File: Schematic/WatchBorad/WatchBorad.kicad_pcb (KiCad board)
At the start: 4 copper layers, 35 x 35 mm, 114 parts, among them J1 Conn_01x07_Female, J3 TYPE-C-31-M-17, M1 Motor_DC, SW1 SW_Push, SW2 SW_Push, SW3 SW_Push, SW4 SW_Push, SW5 SW_Push, U1 LSM6DSLTR, U10 TPS62740DSST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

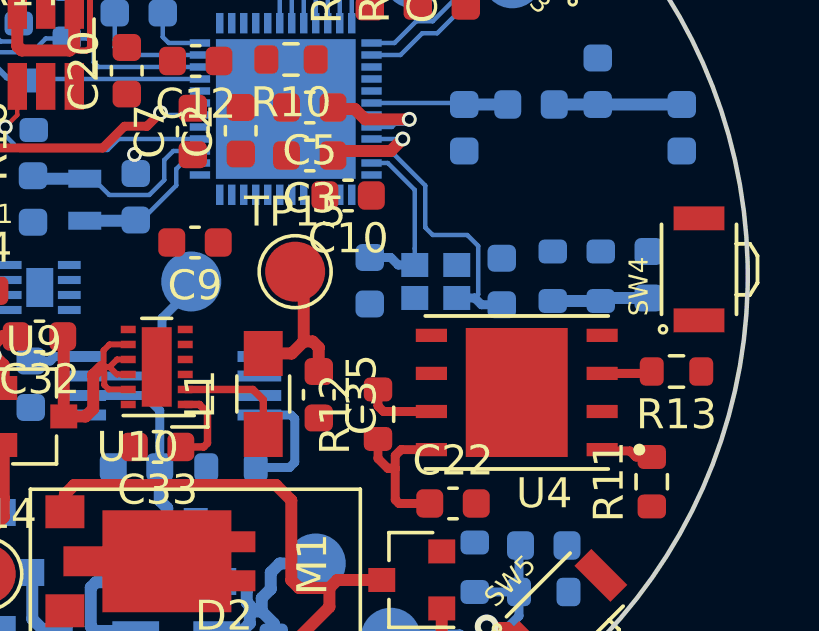
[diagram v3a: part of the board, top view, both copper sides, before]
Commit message: Added route for SPI-FLASH
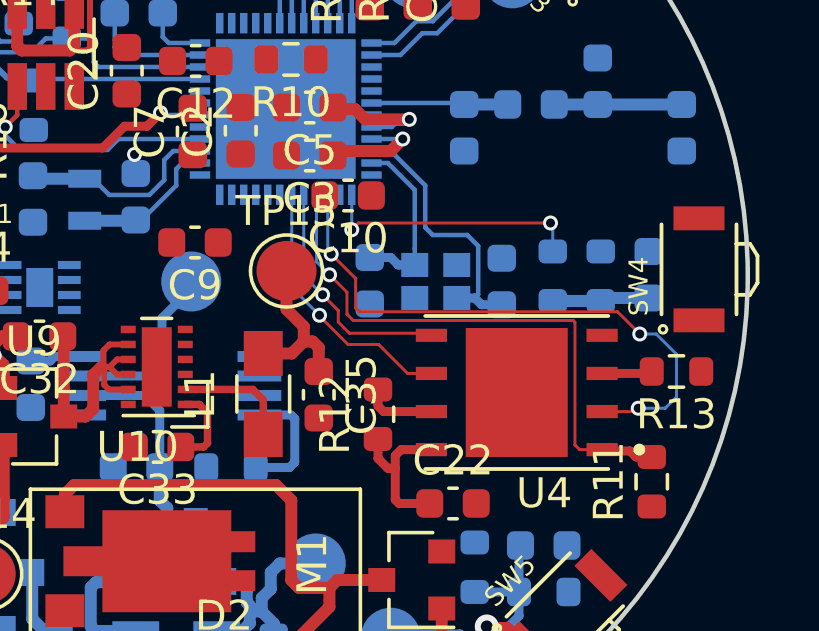
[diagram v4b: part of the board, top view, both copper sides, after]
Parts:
- moved TP15 0.29 mm to (91.0, 88.8)
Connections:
- U2 pad 42: /DCDC&PB/Enable_motor -> /MCU/FLASH_SCK
- U2 pad 43: /MCU/FLASH_SCK -> /DCDC&PB/Enable_motor
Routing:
- net /MCU/FLASH_MISO: track 0.00 -> 19.6 mm, vias 0 -> 3
- net /MCU/FLASH_CS: track 1.76 -> 18.9 mm, vias 0 -> 1
- net /MCU/FLASH_SCK: track 0.00 -> 8.95 mm, vias 0 -> 1
- net /MCU/PB_4_MCU: track 0.00 -> 8.86 mm, vias 0 -> 2
- net /MCU/FLASH_MOSI: track 0.00 -> 8.01 mm, vias 0 -> 1
- net +3V3: track 12.6 -> 13.2 mm
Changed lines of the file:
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@@
     (thickness 1.6)
     (drawings 1)
-    (tracks 450)
+    (tracks 506)
     (zones 0)
     (modules 114)
@@
   )
   (setup
-    (last_trace_width 0.15)
+    (last_trace_width 0.1)
     (user_trace_width 0.1)
     (user_trace_width 0.15)
@@
   )
   (module TestPoint:TestPoint_Pad_D2.0mm (layer F.Cu)
-    (at 91.313 88.773)
+    (at 91.025 88.75)
     (descr "SMD pad as test Point, diameter 2.0mm")
     (tags "test point SMD pad")
@@
       (net 70 "Net-(U2-Pad44)"))
     (pad 43 smd rect (at -0.2 2.86) (size 0.25 0.68) (layers B.Cu B.Paste B.Mask)
-      (net 39 /MCU/FLASH_SCK))
-    (pad 42 smd rect (at 0.2 2.86) (size 0.25 0.68) (layers B.Cu B.Paste B.Mask)
       (net 37 /DCDC&PB/Enable_motor))
+    (pad 42 smd rect (at 0.2 2.86) (size 0.25 0.68) (layers B.Cu B.Paste B.Mask)
+      (net 39 /MCU/FLASH_SCK))
     (pad 41 smd rect (at 0.6 2.86) (size 0.25 0.68) (layers B.Cu B.Paste B.Mask)
       (net 38 /MCU/FLASH_MOSI))
@@
   (segment (start 91.9 91.1) (end 92.1 91.3) (width 0.4) (layer F.Cu) (net 1))
   (segment (start 91.6 89.06) (end 91.313 88.773) (width 0.4) (layer F.Cu) (net 1))
-  (segment (start 91.6 91.1) (end 91.6 89.06) (width 0.4) (layer F.Cu) (net 1))
   (segment (start 94.775 96.5) (end 95.8 96.5) (width 0.3) (layer F.Cu) (net 1))
   (segment (start 94.65 96.375) (end 94.775 96.5) (width 0.3) (layer F.Cu) (net 1))
@@
   (segment (start 94.65 95.325) (end 94.65 96.375) (width 0.3) (layer F.Cu) (net 1))
   (segment (start 94.65 94.9) (end 94.65 95.325) (width 0.3) (layer F.Cu) (net 1))
+  (segment (start 91.025 88.75) (end 91.025 90.025) (width 0.4) (layer F.Cu) (net 1))
+  (segment (start 91.6 90.6) (end 91.6 91.1) (width 0.4) (layer F.Cu) (net 1))
+  (segment (start 91.025 90.025) (end 91.6 90.6) (width 0.4) (layer F.Cu) (net 1))
   (via (at 85.2 77.7) (size 0.5) (drill 0.3) (layers F.Cu B.Cu) (net 2))
   (segment (start 85.3 77.8) (end 85.2 77.7) (width 0.15) (layer B.Cu) (net 2))
@@
   (segment (start 80 93.5) (end 80 92.9) (width 0.4) (layer F.Cu) (net 19))
   (segment (start 79.9 93.6) (end 80 93.5) (width 0.4) (layer F.Cu) (net 19))
+  (via (at 99.825 87.15) (size 0.5) (drill 0.3) (layers F.Cu B.Cu) (net 21))
+  (segment (start 99.9 87.225) (end 99.825 87.15) (width 0.1) (layer B.Cu) (net 21))
+  (segment (start 99.9 88.1) (end 99.9 87.225) (width 0.1) (layer B.Cu) (net 21))
+  (via (at 93.2 87.375) (size 0.5) (drill 0.3) (layers F.Cu B.Cu) (net 21))
+  (segment (start 93.425 87.15) (end 93.2 87.375) (width 0.1) (layer F.Cu) (net 21))
+  (segment (start 99.825 87.15) (end 93.425 87.15) (width 0.1) (layer F.Cu) (net 21))
+  (segment (start 93.2 87.375) (end 93.2 86.21) (width 0.1) (layer B.Cu) (net 21))
   (segment (start 83.95 81.25) (end 83.95 79.9) (width 0.4) (layer F.Cu) (net 23))
   (segment (start 83.8 81.4) (end 83.95 81.25) (width 0.4) (layer F.Cu) (net 23))
@@
   (segment (start 94.575 100.9) (end 94.5 100.975) (width 0.4) (layer B.Cu) (net 37))
   (segment (start 96.8 100.9) (end 94.575 100.9) (width 0.4) (layer B.Cu) (net 37))
+  (via (at 92.227233 89.542614) (size 0.5) (drill 0.3) (layers F.Cu B.Cu) (net 38))
+  (segment (start 91.6 88.915381) (end 92.227233 89.542614) (width 0.1) (layer B.Cu) (net 38))
+  (segment (start 91.6 86.21) (end 91.6 88.915381) (width 0.1) (layer B.Cu) (net 38))
+  (segment (start 92.227233 89.542614) (end 92.75 90.065381) (width 0.1) (layer F.Cu) (net 38))
+  (segment (start 92.75 90.065381) (end 92.75 90.45) (width 0.1) (layer F.Cu) (net 38))
+  (segment (start 92.75 90.45) (end 93.125 90.825) (width 0.1) (layer F.Cu) (net 38))
+  (segment (start 95.785 90.825) (end 95.855 90.895) (width 0.1) (layer F.Cu) (net 38))
+  (segment (start 93.125 90.825) (end 95.785 90.825) (width 0.1) (layer F.Cu) (net 38))
+  (segment (start 95.855 92.165) (end 95.065 92.165) (width 0.1) (layer F.Cu) (net 39))
+  (segment (start 95.065 92.165) (end 94.1 91.2) (width 0.1) (layer F.Cu) (net 39))
+  (segment (start 94.1 91.2) (end 93.075 91.2) (width 0.1) (layer F.Cu) (net 39))
+  (via (at 92.125 90.225) (size 0.5) (drill 0.3) (layers F.Cu B.Cu) (net 39))
+  (segment (start 92.125 90.25) (end 92.125 90.225) (width 0.1) (layer F.Cu) (net 39))
+  (segment (start 93.075 91.2) (end 92.125 90.25) (width 0.1) (layer F.Cu) (net 39))
+  (segment (start 92.125 90.225) (end 91.2 89.3) (width 0.1) (layer B.Cu) (net 39))
+  (segment (start 91.2 87.05) (end 91.2 86.21) (width 0.1) (layer B.Cu) (net 39))
+  (segment (start 91.2 89.3) (end 91.2 87.05) (width 0.1) (layer B.Cu) (net 39))
+  (via (at 102.75 93.325) (size 0.5) (drill 0.3) (layers F.Cu B.Cu) (net 40))
+  (segment (start 102.64 93.435) (end 102.75 93.325) (width 0.1) (layer F.Cu) (net 40))
+  (segment (start 101.545 93.435) (end 102.64 93.435) (width 0.1) (layer F.Cu) (net 40))
+  (segment (start 102.75 93.325) (end 103.65 93.325) (width 0.1) (layer B.Cu) (net 40))
+  (segment (start 103.65 93.325) (end 104.025 92.95) (width 0.1) (layer B.Cu) (net 40))
+  (segment (start 104.025 92.95) (end 104.025 91.525) (width 0.1) (layer B.Cu) (net 40))
+  (via (at 102.8 90.85) (size 0.5) (drill 0.3) (layers F.Cu B.Cu) (net 40))
+  (segment (start 103.35 90.85) (end 102.8 90.85) (width 0.1) (layer B.Cu) (net 40))
+  (segment (start 104.025 91.525) (end 103.35 90.85) (width 0.1) (layer B.Cu) (net 40))
+  (segment (start 102.8 90.85) (end 102.05999 90.10999) (width 0.1) (layer F.Cu) (net 40))
+  (segment (start 93.45999 90.10999) (end 93.33002 89.98002) (width 0.1) (layer F.Cu) (net 40))
+  (segment (start 102.05999 90.10999) (end 93.45999 90.10999) (width 0.1) (layer F.Cu) (net 40))
+  (segment (start 93.33002 89.98002) (end 93.33002 89.25502) (width 0.1) (layer F.Cu) (net 40))
+  (via (at 92.515 88.187136) (size 0.5) (drill 0.3) (layers F.Cu B.Cu) (net 40))
+  (segment (start 93.33002 89.002156) (end 92.515 88.187136) (width 0.1) (layer F.Cu) (net 40))
+  (segment (start 93.33002 89.25502) (end 93.33002 89.002156) (width 0.1) (layer F.Cu) (net 40))
+  (segment (start 92.4 88.072136) (end 92.4 86.21) (width 0.1) (layer B.Cu) (net 40))
+  (segment (start 92.515 88.187136) (end 92.4 88.072136) (width 0.1) (layer B.Cu) (net 40))
   (segment (start 103.2 94.95) (end 102.675 94.95) (width 0.3) (layer F.Cu) (net 41))
   (segment (start 102.675 94.95) (end 102.475 94.75) (width 0.3) (layer F.Cu) (net 41))
   (segment (start 101.59 94.75) (end 101.545 94.705) (width 0.3) (layer F.Cu) (net 41))
   (segment (start 102.475 94.75) (end 101.59 94.75) (width 0.3) (layer F.Cu) (net 41))
+  (via (at 92.459403 88.876862) (size 0.5) (drill 0.3) (layers F.Cu B.Cu) (net 41))
+  (segment (start 92.459403 88.876862) (end 92.025 88.442459) (width 0.1) (layer B.Cu) (net 41))
+  (segment (start 92.025 86.235) (end 92 86.21) (width 0.1) (layer B.Cu) (net 41))
+  (segment (start 92.025 88.442459) (end 92.025 86.235) (width 0.1) (layer B.Cu) (net 41))
+  (segment (start 93.04001 89.457469) (end 92.459403 88.876862) (width 0.1) (layer F.Cu) (net 41))
+  (segment (start 93.04001 90.19001) (end 93.04001 89.457469) (width 0.1) (layer F.Cu) (net 41))
+  (segment (start 93.25 90.4) (end 93.04001 90.19001) (width 0.1) (layer F.Cu) (net 41))
+  (segment (start 100.582002 90.4) (end 93.25 90.4) (width 0.1) (layer F.Cu) (net 41))
+  (segment (start 100.640001 90.457999) (end 100.582002 90.4) (width 0.1) (layer F.Cu) (net 41))
+  (segment (start 100.640001 94.55) (end 100.640001 90.457999) (width 0.1) (layer F.Cu) (net 41))
+  (segment (start 100.795001 94.705) (end 100.640001 94.55) (width 0.1) (layer F.Cu) (net 41))
+  (segment (start 101.545 94.705) (end 100.795001 94.705) (width 0.1) (layer F.Cu) (net 41))
   (segment (start 88.14 84.35) (end 85.425 84.35) (width 0.15) (layer B.Cu) (net 42))
   (via (at 81.65 83.95) (size 0.5) (drill 0.3) (layers F.Cu B.Cu) (net 42))

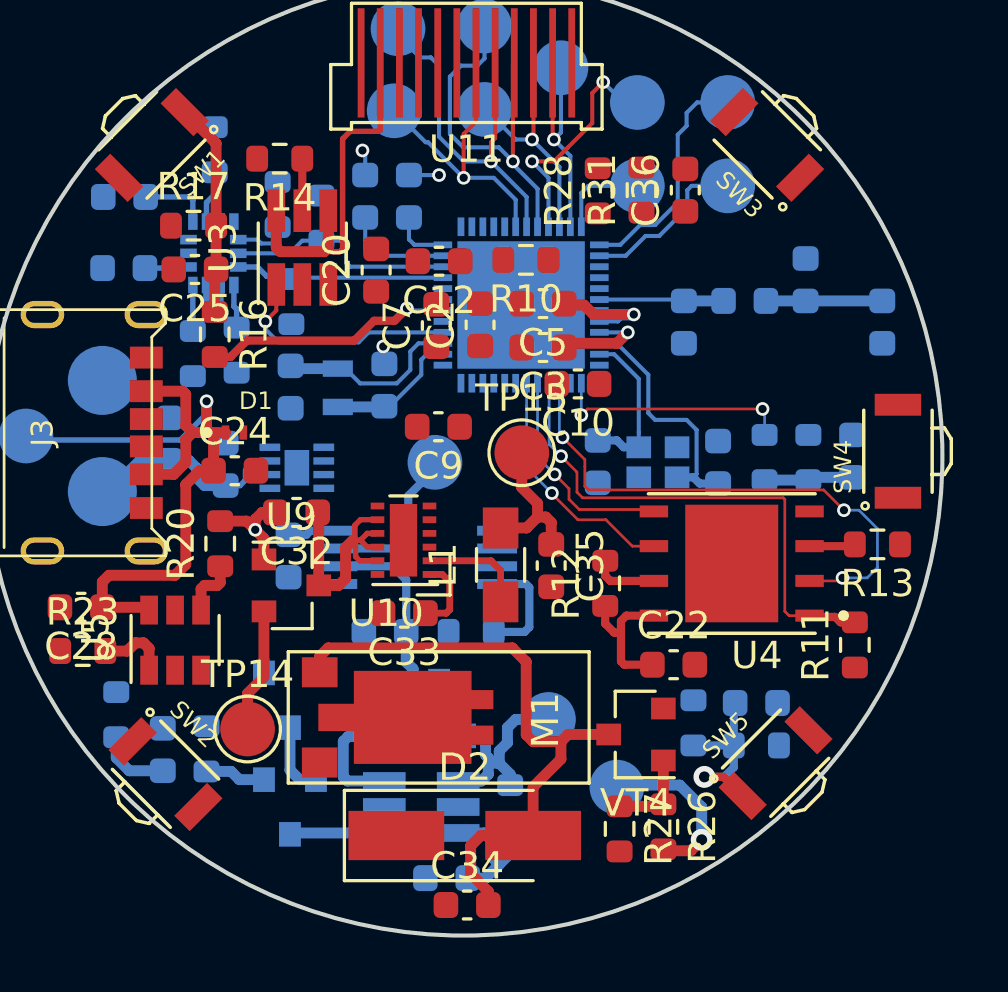
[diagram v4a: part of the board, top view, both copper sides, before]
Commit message: Added routing for power plane
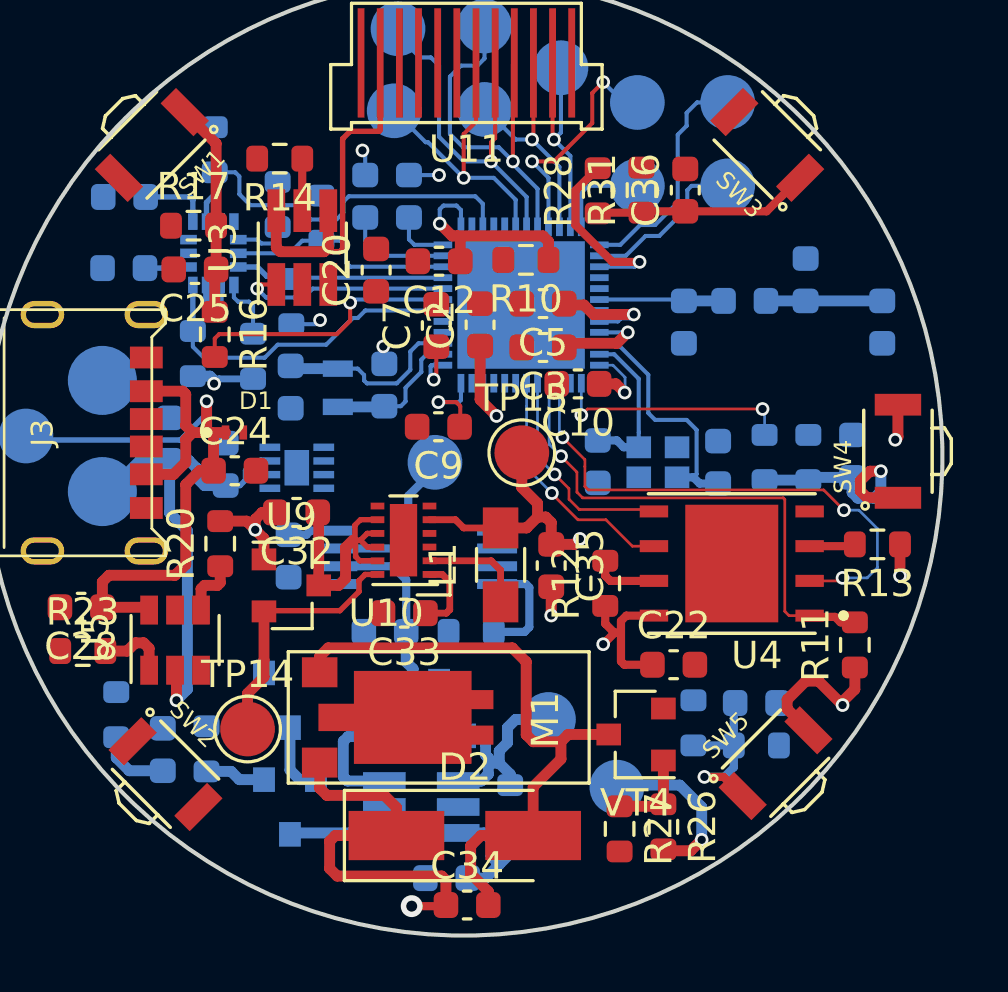
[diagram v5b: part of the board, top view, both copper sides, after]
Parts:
- moved R5 0.64 mm to (81.2, 85.2)
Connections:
- U2 pad 14: /MCU/MPU_INT_1 -> /MCU/P5
- U2 pad 4: /MCU/Backlight_EN_DIM -> /MCU/P6
- U2 pad 6: /MCU/PB_2_MCU -> /MCU/MPU_INT_1
- U2 pad 7: /MCU/P5 -> /MCU/PB_2_MCU
- U2 pad 8: /MCU/P6 -> /MCU/Backlight_EN_DIM
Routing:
- net +3V3: track 13.2 -> 129.2 mm, vias 0 -> 11
- net /MCU/MPU_INT_2: track 1.92 -> 14.7 mm
- net /MCU/MPU_INT_1: track 1.68 -> 12.3 mm
- net +BATT: track 13.8 -> 24.2 mm, vias 0 -> 1
- net Net-(C36-Pad1): track 0.00 -> 7.94 mm
- net /MCU/PB_3_MCU: track 0.00 -> 6.86 mm, vias 0 -> 1
- net Net-(C37-Pad1): track 3.24 -> 8.52 mm, vias 0 -> 1
- net /DCDC&PB/DCDC_ENABLE: track 4.55 -> 9.49 mm
- net /MCU/DEC4: track 0.00 -> 4.21 mm, vias 0 -> 1
- net /MCU/DEC1: track 0.00 -> 2.49 mm, vias 0 -> 1
- net GND: track 6.54 -> 7.59 mm, vias 4 -> 5
- net /MCU/PB_2_MCU: track 9.13 -> 9.99 mm
- net /MCU/Backlight_EN_DIM: track 8.64 -> 7.82 mm
- net Net-(R5-Pad2): track 1.60 -> 2.30 mm

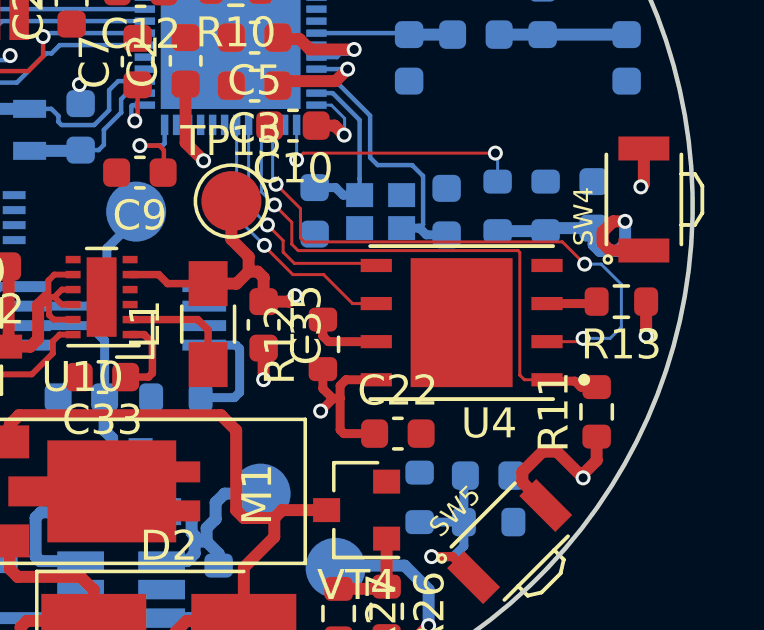
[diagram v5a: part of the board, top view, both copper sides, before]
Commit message: Added testpoints for SPI-FLASH
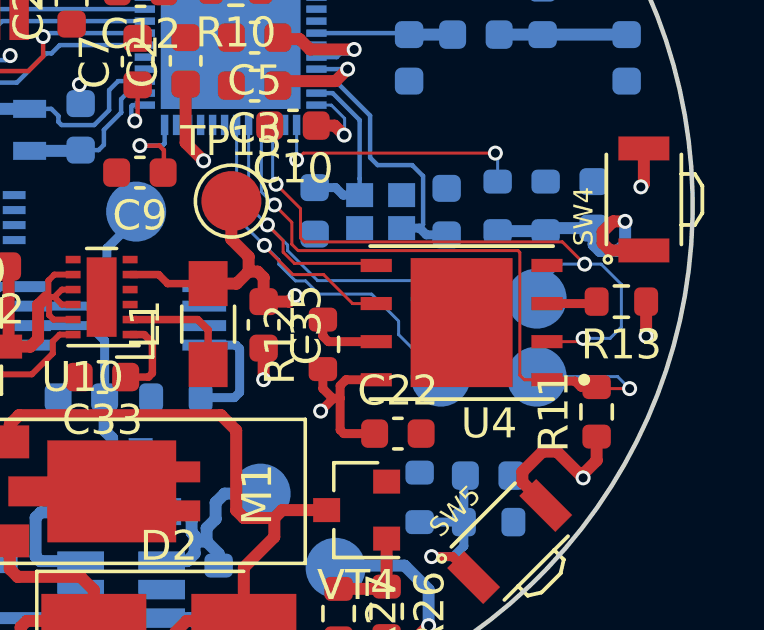
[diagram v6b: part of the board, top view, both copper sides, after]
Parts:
- added TP16: TestPoint, TestPoint:TestPoint_Pad_D2.0mm, B.Cu at (101.2, 92.0)
- added TP17: TestPoint, TestPoint:TestPoint_Pad_D2.0mm, B.Cu at (101.2, 94.6)
- added TP18: TestPoint, TestPoint:TestPoint_Pad_D2.0mm, B.Cu at (98.0, 92.0)
- added TP19: TestPoint, TestPoint:TestPoint_Pad_D2.0mm, B.Cu at (98.0, 94.6)
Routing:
- net /MCU/FLASH_SCK: track 8.95 -> 17.0 mm
- net /MCU/FLASH_MOSI: track 8.01 -> 14.9 mm
- net /MCU/FLASH_CS: track 18.9 -> 23.3 mm, vias 1 -> 2
- net /MCU/FLASH_MISO: track 19.6 -> 22.7 mm

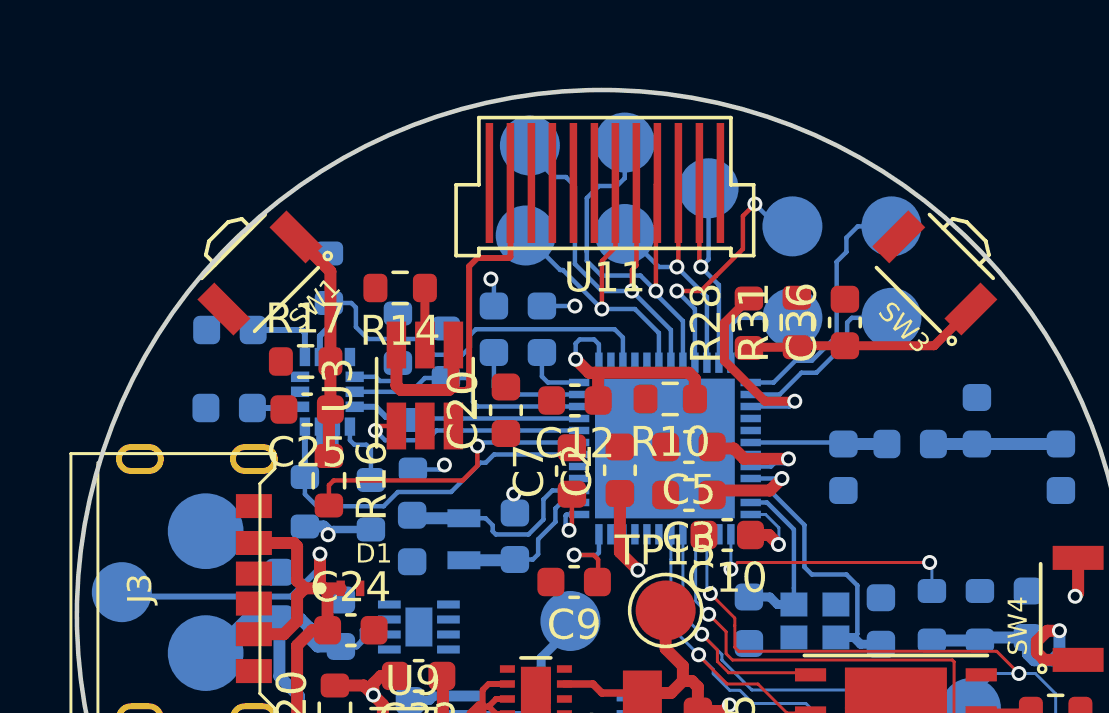
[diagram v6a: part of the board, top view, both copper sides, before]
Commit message: Finished 3V3 routing
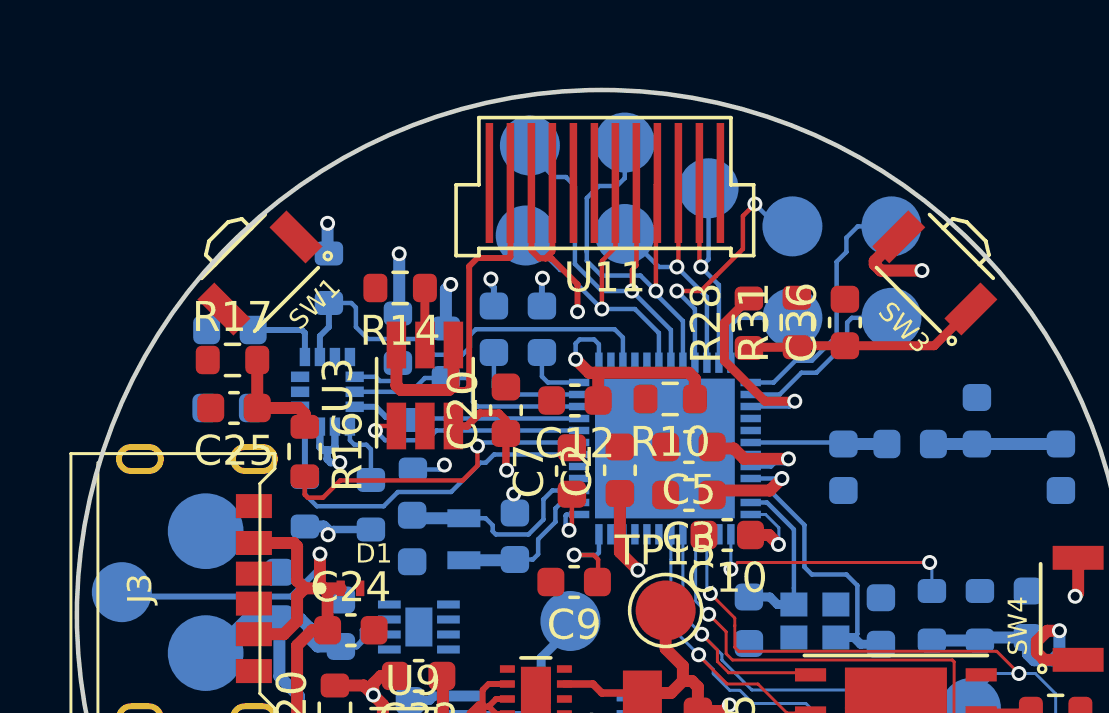
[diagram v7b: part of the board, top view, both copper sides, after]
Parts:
- moved C25 2.44 mm to (76.6, 82.0)
- moved R17 2.44 mm to (76.6, 80.4)
- moved R16 1.26 mm to (79.0, 83.5)
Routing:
- net +3V3: track 129.2 -> 183.4 mm, vias 11 -> 18
- net Net-(C25-Pad1): track 7.80 -> 3.77 mm
- net /MCU/PB_2_MCU: track 9.99 -> 10.9 mm
